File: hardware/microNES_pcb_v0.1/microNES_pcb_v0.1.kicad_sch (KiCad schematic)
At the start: 105 parts, among them J1 USB_C_Receptacle_USB2.0_16P, J3 HDMI_E, J4 SM03B-SRSS-TB, J5 Conn_01x05, Q1 2N7002, SW3 PTS810SJM250SMTRLFS, SW4 PTS810SJM250SMTRLFS, U1 RP2350_60QFN, U2 AMS1117-3.3, U3 W25Q128JVS, U5 AMS1117-3.3, Y1 ABM8-272-T3

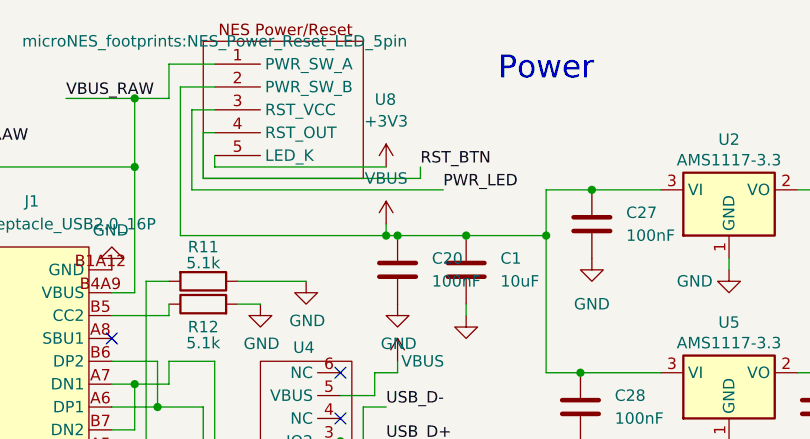
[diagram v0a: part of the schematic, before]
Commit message: MicroNES full PCB! Wire up the v0.1 PCB peripherals (#29)
* Pico: derive peripheral pin assignments from PCB v0.1 schematic

Add a canonical board pinout header sourced from
hardware/microNES_pcb_v0.1/microNES_pcb_v0.1.kicad_sch, and a
MICRONES_BOARD CMake option (breadboard|v0_1) that drives it into
every Pico pin header.  Default behaviour is unchanged.

With -DMICRONES_BOARD=v0_1 the firmware now uses the silkscreen
nets: video DAC on GP24-27 (GP_VDAC_SUM0..3) with sync clamp on
GP28 (GP_VDAC_GATE); audio PWM on GP23 (GP_ADAC_IN); NES
controller on GP6/7/8 (NES_CLOCK/LATCH/DATA_1); SD card on
GP1-5 (unchanged, already matched the PCB).

* Pico: read both NES controllers from the v0.1 PCB

The v0.1 PCB routes a second 4021 controller port: CLOCK and LATCH are
shared with player 1 on GP6/GP7, and a second DATA line comes back on
GP9 (NES_DATA_2).  Reading both ports therefore costs the same eight
clock edges as reading one — only the GPIO sample inside the shift
loop changes.

Extend the platform driver with nes_hw_controller_read_pair() that
samples both DATA lines per shift step, and surface it through
pico_input_read_pair() returning a {p1, p2} struct.  main.c reads the
pair each frame: player 1 still drives the AppShell (menu nav and
exit combo), player 2 is routed straight to NES controller port 2
($4017).  On boards without PICO_NES_CTL_DATA_P2 (breadboard
default) the second port is reported as "no buttons", so existing
single-port behaviour is preserved.

The NES core already exposed controllers[2], so no emulator changes
were required.  The ESP32-S3 reference driver gains a one-port
wrapper for source-compatibility.

* Pico: drive PWR_LED and read RST_BTN on the v0.1 PCB

Add a small pico_status module that brings up the v0.1 front-panel I/O:

* GP21 (PWR_LED) — configured as output and driven to the lit state in
  pico_status_init(), so the panel LED comes on as soon as the firmware
  reaches the bring-up phase.  Defaults to active-HIGH (common-anode
  pa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
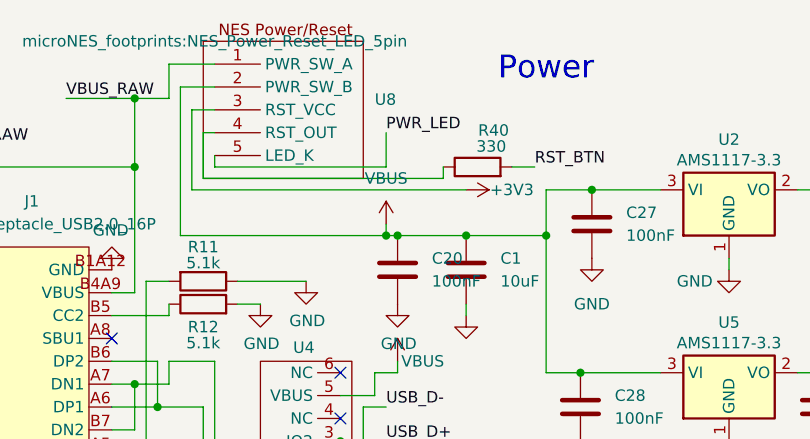
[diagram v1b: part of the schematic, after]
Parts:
- added R40: 330, Resistor_SMD:R_0402_1005Metric, symbol Device:R
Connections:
- net +3V3: now also U8.3 (RST_VCC); no longer U8.5 (LED_K)
- net PWR_LED: now also U8.5 (LED_K); no longer U8.3 (RST_VCC)
- net RST_BTN: now also R40.2; no longer U8.4 (RST_OUT)
- new net: R40.1, U8.4 (RST_OUT)
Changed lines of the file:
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@@
 	(wire
 		(pts
-			(xy 59.69 30.48) (xy 83.82 30.48)
+			(xy 59.69 30.48) (xy 86.36 30.48)
 		)
 		(stroke
@@
 	(wire
 		(pts
+			(xy 96.52 29.21) (xy 93.98 29.21)
+		)
+		(stroke
+			(width 0)
+			(type default)
+		)
+	)
+	(wire
+		(pts
 			(xy 271.78 92.71) (xy 275.59 92.71)
 		)
@@
 	(wire
 		(pts
-			(xy 83.82 29.21) (xy 83.82 30.48)
+			(xy 86.36 29.21) (xy 86.36 30.48)
 		)
 		(stroke
@@
 	(wire
 		(pts
+			(xy 80.01 25.4) (xy 80.01 29.21)
+		)
+		(stroke
+			(width 0)
+			(type default)
+		)
+	)
+	(wire
+		(pts
 			(xy 184.15 63.5) (xy 176.53 63.5)
 		)
@@
 	(wire
 		(pts
-			(xy 58.42 31.75) (xy 86.36 31.75)
+			(xy 58.42 31.75) (xy 88.9 31.75)
 		)
 		(stroke
@@
 		)
 	)
+	(label "PWR_LED"
+		(at 80.01 25.4 0)
+		(effects
+			(font
+				(size 1.27 1.27)
+			)
+			(justify left bottom)
+		)
+	)
 	(label "QSPI_SD0"
 		(at 153.67 96.52 180)
@@
 		)
 	)
-	(label "PWR_LED"
-		(at 86.36 31.75 0)
-		(effects
-			(font
-				(size 1.27 1.27)
-			)
-			(justify left bottom)
-		)
-	)
 	(label "CARD_CMD"
 		(at 378.46 102.87 180)
@@
 		)
 	)
-	(label "RST_BTN"
-		(at 83.82 29.21 0)
-		(effects
-			(font
-				(size 1.27 1.27)
-			)
-			(justify left bottom)
-		)
-	)
 	(label "GP_ADAC_IN"
 		(at 304.8 195.58 90)
@@
 		)
 	)
+	(label "RST_BTN"
+		(at 96.52 29.21 0)
+		(effects
+			(font
+				(size 1.27 1.27)
+			)
+			(justify left bottom)
+		)
+	)
 	(label "NES_LATCH"
 		(at 72.39 224.79 0)
@@
 	)
 	(symbol
+		(lib_id "Device:R")
+		(at 90.17 29.21 90)
+		(unit 1)
+		(body_style 1)
+		(exclude_from_sim no)
+		(in_bom yes)
+		(on_board yes)
+		(in_pos_files yes)
+		(dnp no)
+		(property "Reference" "R40"
+			(at 91.948 25.146 90)
+			(show_name no)
+			(do_not_autoplace no)
+			(effects
+				(font
+					(size 1.27 1.27)
+				)
+			)
+		)
+		(property "Value" "330"
+			(at 91.694 26.924 90)
+			(show_name no)
+			(do_not_autoplace no)
+			(effects
+				(font
+					(size 1.27 1.27)
+				)
+			)
+		)
+		(property "Footprint" "Resistor_SMD:R_0402_1005Metric"
+			(at 90.17 30.988 90)
+			(hide yes)
+			(show_name no)
+			(do_not_autoplace no)
+			(effects
+				(font
+					(size 1.27 1.27)
+				)
+			)
+		)
+		(property "Datasheet" ""
+			(at 90.17 29.21 0)
+			(hide yes)
+			(show_name no)
+			(do_not_autoplace no)
+			(effects
+				(font
+					(size 1.27 1.27)
+				)
+			)
+		)
+		(property "Description" "Resistor"
+			(at 90.17 29.21 0)
+			(hide yes)
+			(show_name no)
+			(do_not_autoplace no)
+			(effects
+				(font
+					(size 1.27 1.27)
+				)
+			)
+		)
+		(property "LCSC" "C25104"
+			(at 90.17 29.21 90)
+			(hide yes)
+			(show_name no)
+			(do_not_autoplace no)
+			(effects
+				(font
+					(size 1.27 1.27)
+				)
+			)
+		)
+		(pin "2"
+		)
+		(pin "1"
+		)
+		(instances
+			(project "microNES_pcb_v0.1"
+				(path "/aba63da5-2856-45d3-bb43-ffaad5b78152"
+					(reference "R40")
+					(unit 1)
+				)
+			)
+		)
+	)
+	(symbol
 		(lib_id "Device:C")
 		(at 335.28 81.28 0)
@@
 	)
 	(symbol
+		(lib_name "+3V3_9")
+		(lib_id "power:+3V3")
+		(at 88.9 31.75 270)
+		(unit 1)
+		(body_style 1)
+		(exclude_from_sim no)
+		(in_bom yes)
+		(on_board yes)
+		(in_pos_files yes)
+		(dnp no)
+		(property "Reference" "#PWR041"
+			(at 85.09 31.75 0)
+			(hide yes)
+			(show_name no)
+			(do_not_autoplace no)
+			(effects
+				(font
+					(size 1.27 1.27)
+				)
+			)
+		)
+		(property "Value" "+3V3"
+			(at 93.98 31.75 90)
+			(show_name no)
+			(do_not_autoplace no)
+			(effects
+				(font
+					(size 1.27 1.27)
+				)
+			)
+		)
+		(property "Footprint" ""
+			(at 88.9 31.75 0)
+			(hide yes)
+			(show_name no)
+			(do_not_autoplace no)
+			(effects
+				(font
+					(size 1.27 1.27)
+				)
+			)
+		)
+		(property "Datasheet" ""
+			(at 88.9 31.75 0)
+			(hide yes)
+			(show_name no)
+			(do_not_autoplace no)
+			(effects
+				(font
+					(size 1.27 1.27)
+				)
+			)
+		)
+		(property "Description" "Power symbol creates a global label with name \"+3V3\""
+			(at 88.9 31.75 0)
+			(hide yes)
+			(show_name no)
+			(do_not_autoplace no)
+			(effects
+				(font
+					(size 1.27 1.27)
+				)
+			)
+		)
+		(pin "1"
+		)
+		(instances
+			(project "microNES_pcb_v0.1"
+				(path "/aba63da5-2856-45d3-bb43-ffaad5b78152"
+					(reference "#PWR041")
+					(unit 1)
+				)
+			)
+		)
+	)
+	(symbol
 		(lib_id "power:GND")
 		(at 335.28 86.36 0)
@@
 					(unit 1)
 				)
-			)
-		)
-	)
-	(symbol
-		(lib_name "+3V3_9")
-		(lib_id "power:+3V3")
-		(at 80.01 29.21 0)
-		(unit 1)
-		(body_style 1)
-		(exclude_from_sim no)
-		(in_bom yes)
-		(on_board yes)
-		(in_pos_files yes)
-		(dnp no)
-		(fields_autoplaced yes)
-		(property "Reference" "#PWR085"
-			(at 80.01 33.02 0)
-			(hide yes)
-			(show_name no)
-			(do_not_autoplace no)
-			(effects
-				(font
-					(size 1.27 1.27)
-				)
-			)
-		)
-		(property "Value" "+3V3"
-			(at 80.01 24.13 0)
-			(show_name no)
-			(do_not_autoplace no)
-			(effects
-				(font
-					(size 1.27 1.27)
-				)
-			)
-		)
-		(property "Footprint" ""
-			(at 80.01 29.21 0)
-			(hide yes)
-			(show_name no)
-			(do_not_autoplace no)
-			(effects
-				(font
-					(size 1.27 1.27)
-				)
-			)
-		)
-		(property "Datasheet" ""
-			(at 80.01 29.21 0)
-			(hide yes)
-			(show_name no)
-			(do_not_autoplace no)
-			(effects
-				(font
-					(size 1.27 1.27)
-				)
-			)
-		)
-		(property "Description" "Power symbol creates a global label with name \"+3V3\""
-			(at 80.01 29.21 0)
-			(hide yes)
-			(show_name no)
-			(do_not_autoplace no)
-			(effects
-				(font
-					(size 1.27 1.27)
-				)
-			)
-		)
-		(pin "1"
-		)
-		(instances
-			(project "microNES_pcb_v0.1"
-				(path "/aba63da5-2856-45d3-bb43-ffaad5b78152"
-					(reference "#PWR085")
-					(unit 1)
-				)
